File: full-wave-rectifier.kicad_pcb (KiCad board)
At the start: 2 copper layers, 80.6 x 108 mm, 0 parts

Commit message: save changes
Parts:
- added C1: 10uF, Capacitor_THT:CP_Radial_D5.0mm_P2.00mm, B.Cu at (171.4, 137.2)
- added C10: 100nF, Capacitor_SMD:C_1206_3216Metric, F.Cu at (184.2, 68.6)
- added C11: 100nF, Capacitor_SMD:C_1206_3216Metric, F.Cu at (171.4, 101.6)
- added C12: 100nF, Capacitor_SMD:C_1206_3216Metric, F.Cu at (184.2, 101.6)
- added C13: 100nF, Capacitor_SMD:C_1206_3216Metric, F.Cu at (171.4, 127.0)
- added C14: 100nF, Capacitor_SMD:C_1206_3216Metric, F.Cu at (184.2, 127.0)
- added C15: 1uF_Radial_TH, Capacitor_THT:C_Rect_L7.2mm_W4.5mm_P5.00mm_FKS2_FKP2_MKS2_MKP2, F.Cu at (207.4, 77.5)
- added C2: 10uF, Capacitor_THT:CP_Radial_D5.0mm_P2.00mm, B.Cu at (182.2, 137.2)
- added C3: 10uF, Capacitor_THT:CP_Radial_D5.0mm_P2.00mm, F.Cu at (201.3, 68.4)
- added C4: 10uF, Capacitor_THT:CP_Radial_D5.0mm_P2.00mm, F.Cu at (201.3, 75.0)
- added C5: 100nF, Capacitor_SMD:C_1206_3216Metric, F.Cu at (165.1, 142.0)
- added C6: 100nF, Capacitor_SMD:C_1206_3216Metric, F.Cu at (190.5, 142.0)
- added C7: 100nF, Capacitor_THT:C_Disc_D4.3mm_W1.9mm_P5.00mm, F.Cu at (215.9, 76.2)
- added C8: 100nF, Capacitor_THT:C_Disc_D4.3mm_W1.9mm_P5.00mm, F.Cu at (215.9, 79.7)
- added C9: 100nF, Capacitor_SMD:C_1206_3216Metric, F.Cu at (171.4, 68.6)
- added D3: 1N4148, Diode_THT:D_DO-35_SOD27_P7.62mm_Horizontal, F.Cu at (177.8, 24.4)
- added D4: 1N4148, Diode_THT:D_DO-35_SOD27_P7.62mm_Horizontal, F.Cu at (177.8, 27.9)
- added D5: 1N4148, Diode_THT:D_DO-35_SOD27_P7.62mm_Horizontal, F.Cu at (177.8, 31.5)
- added D6: 1N4148, Diode_THT:D_DO-35_SOD27_P7.62mm_Horizontal, F.Cu at (177.8, 35.0)
- added FB1: FerriteBead, Inductor_SMD:L_1206_3216Metric_Pad1.22x1.90mm_HandSolder, F.Cu at (188.8, 146.1)
- added FB2: FerriteBead, Inductor_SMD:L_1206_3216Metric_Pad1.22x1.90mm_HandSolder, F.Cu at (165.1, 150.7)
- added J10: Control Right, Connector_PinSocket_2.54mm:PinSocket_1x08_P2.54mm_Vertical, B.Cu at (139.7, 94.0)
- added J11: Main Right, Connector_PinHeader_2.54mm:PinHeader_1x08_P2.54mm_Vertical, F.Cu at (190.5, 94.0)
- added J12: Power Connector, Connector_IDC:IDC-Header_2x05_P2.54mm_Vertical, B.Cu at (182.9, 147.3)
- added J2: Input Ch1, AudioJacks:Jack_3.5mm_QingPu_WQP-PJ398SM_Vertical, F.Cu at (121.9, 131.9)
- added J3: Input Ch2, AudioJacks:Jack_3.5mm_QingPu_WQP-PJ398SM_Vertical, F.Cu at (132.1, 131.9)
- added J4: Output Ch1, AudioJacks:Jack_3.5mm_QingPu_WQP-PJ398SM_Vertical, F.Cu at (121.9, 147.2)
- added J5: Output Ch2, AudioJacks:Jack_3.5mm_QingPu_WQP-PJ398SM_Vertical, F.Cu at (132.1, 147.2)
- added J6: Ochd input, Connector_PinHeader_2.54mm:PinHeader_1x02_P2.54mm_Vertical, B.Cu at (139.7, 119.4)
- added J8: Control Left, Connector_PinSocket_2.54mm:PinSocket_1x08_P2.54mm_Vertical, B.Cu at (114.3, 94.0)
- added J9: Main Left, Connector_PinHeader_2.54mm:PinHeader_1x08_P2.54mm_Vertical, F.Cu at (165.1, 94.0)
- added POT1: 9mm_NoDet_10k_DShaft, Potentiometer_THT:Potentiometer_Alpha_RD901F-40-00D_Single_Vertical, F.Cu at (124.5, 61.0)
- added POT2: 9mm_NoDet_10k_DShaft, Potentiometer_THT:Potentiometer_Alpha_RD901F-40-00D_Single_Vertical, F.Cu at (124.5, 81.3)
- added POT3: 9mm_NoDet_10k_DShaft, Potentiometer_THT:Potentiometer_Alpha_RD901F-40-00D_Single_Vertical, F.Cu at (124.5, 101.6)
- added POT4: 9mm_NoDet_10k_DShaft, Potentiometer_THT:Potentiometer_Alpha_RD901F-40-00D_Single_Vertical, F.Cu at (124.5, 121.9)
- added Q7: AO3404A, Package_TO_SOT_SMD:SOT-23_Handsoldering, F.Cu at (184.4, 151.4)
- added Q8: AO3407A, Package_TO_SOT_SMD:SOT-23_Handsoldering, F.Cu at (171.2, 151.4)
- added R1: 100k, Resistor_SMD:R_1206_3216Metric, F.Cu at (168.9, 145.9)
- added R10: 100k_TH0.125, Resistor_THT:R_Axial_DIN0207_L6.3mm_D2.5mm_P2.54mm_Vertical, F.Cu at (86.6, 39.9)
- added R11: 100k_TH0.125, Resistor_THT:R_Axial_DIN0207_L6.3mm_D2.5mm_P2.54mm_Vertical, F.Cu at (86.6, 43.9)
- added R12: 100k_TH0.125, Resistor_THT:R_Axial_DIN0207_L6.3mm_D2.5mm_P2.54mm_Vertical, F.Cu at (92.7, 27.7)
- added R13: 100k_TH0.125, Resistor_THT:R_Axial_DIN0207_L6.3mm_D2.5mm_P2.54mm_Vertical, F.Cu at (92.7, 31.8)
- added R14: 100k_TH0.125, Resistor_THT:R_Axial_DIN0207_L6.3mm_D2.5mm_P2.54mm_Vertical, F.Cu at (92.7, 35.8)
- added R15: 100k_TH0.125, Resistor_THT:R_Axial_DIN0207_L6.3mm_D2.5mm_P2.54mm_Vertical, F.Cu at (92.7, 39.9)
- added R16: 100k_TH0.125, Resistor_THT:R_Axial_DIN0207_L6.3mm_D2.5mm_P2.54mm_Vertical, F.Cu at (92.7, 43.9)
- added R17: 100k_TH0.125, Resistor_THT:R_Axial_DIN0207_L6.3mm_D2.5mm_P2.54mm_Vertical, F.Cu at (98.8, 27.7)
- added R18: 100k_TH0.125, Resistor_THT:R_Axial_DIN0207_L6.3mm_D2.5mm_P2.54mm_Vertical, F.Cu at (98.8, 31.8)
- added R19: 100k_TH0.125, Resistor_THT:R_Axial_DIN0207_L6.3mm_D2.5mm_P2.54mm_Vertical, F.Cu at (98.8, 35.8)
- added R2: 100k, Resistor_SMD:R_1206_3216Metric, F.Cu at (190.5, 150.9)
- added R20: 100k_TH0.125, Resistor_THT:R_Axial_DIN0207_L6.3mm_D2.5mm_P2.54mm_Vertical, F.Cu at (98.8, 39.9)
- added R21: 51k_TH0.125, Resistor_THT:R_Axial_DIN0207_L6.3mm_D2.5mm_P5.08mm_Vertical, F.Cu at (160.0, 33.3)
- added R22: 51k_TH0.125, Resistor_THT:R_Axial_DIN0207_L6.3mm_D2.5mm_P5.08mm_Vertical, F.Cu at (160.0, 37.3)
- added R23: 100Ω_TH0.125, Resistor_THT:R_Axial_DIN0207_L6.3mm_D2.5mm_P2.54mm_Vertical, F.Cu at (207.6, 82.5)
- added R3: 100k_TH0.125, Resistor_THT:R_Axial_DIN0207_L6.3mm_D2.5mm_P2.54mm_Vertical, F.Cu at (108.0, 134.6)
- added R4: 100k_TH0.125, Resistor_THT:R_Axial_DIN0207_L6.3mm_D2.5mm_P2.54mm_Vertical, F.Cu at (134.6, 106.7)
- added R5: 1k_TH0.125, Resistor_THT:R_Axial_DIN0207_L6.3mm_D2.5mm_P5.08mm_Vertical, F.Cu at (105.4, 129.5)
- added R6: 1k_TH0.125, Resistor_THT:R_Axial_DIN0207_L6.3mm_D2.5mm_P5.08mm_Vertical, F.Cu at (134.6, 116.6)
- added R7: 1k_TH0.125, Resistor_THT:R_Axial_DIN0207_L6.3mm_D2.5mm_P5.08mm_Vertical, F.Cu at (103.1, 152.4)
- added R8: 1k_TH0.125, Resistor_THT:R_Axial_DIN0207_L6.3mm_D2.5mm_P5.08mm_Vertical, F.Cu at (143.7, 152.4)
- added R9: 100k_TH0.125, Resistor_THT:R_Axial_DIN0207_L6.3mm_D2.5mm_P2.54mm_Vertical, F.Cu at (86.6, 35.8)
- added U1: LM78L05_TO92, Package_TO_SOT_THT:TO-92_Inline_Wide, F.Cu at (219.1, 64.9)
- added U2: TL074, Package_SO:SOIC-14_3.9x8.7mm_P1.27mm, F.Cu at (177.8, 127.0)
- added U3: TL074, Package_SO:SOIC-14_3.9x8.7mm_P1.27mm, F.Cu at (177.8, 101.6)
- added U4: TL074, Package_SO:SOIC-14_3.9x8.7mm_P1.27mm, F.Cu at (177.8, 68.6)
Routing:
- net +12V: track 0.00 -> 100.9 mm
- net -12V: track 0.00 -> 97.9 mm
- net Net-(Q8-D): track 0.00 -> 6.67 mm
- net Net-(Q7-D): track 0.00 -> 6.67 mm
- net Net-(Q7-S): track 0.00 -> 4.99 mm
- net Net-(Q8-S): track 0.00 -> 4.62 mm
- net Net-(Q7-G): track 0.00 -> 4.62 mm
- net Net-(Q8-G): track 0.00 -> 3.52 mm
- added copper zone on B.Cu, net GND
- added copper zone on F.Cu, net GND
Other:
- outline, holes or cut-outs redrawn

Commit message: save changes
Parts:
- moved R7 37.4 mm to (118.1, 118.1), turned to -90 degrees
- moved R8 35.2 mm to (135.9, 118.1), turned to -90 degrees
- moved R3 31.2 mm to (121.9, 106.7)
- moved R5 19.8 mm to (118.1, 114.3), turned to 90 degrees
- moved R6 2.64 mm to (135.9, 114.3)
- moved R4 2.54 mm to (132.1, 106.7)
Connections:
- POT1 pad 1: /T_Output_1 -> Net-(POT1A-Left)
- POT2 pad 1: /T_Offset_1 -> Net-(POT2A-Left)
- POT3 pad 1: /T_Output_2 -> Net-(POT3A-Left)
- POT4 pad 1: /T_Offset_2 -> Net-(POT4A-Left)
- R13 pad 1: INPUT_CH1 -> Net-(U3D--)
- R14 pad 2: INPUT_CH1 -> Net-(U3D--)
- R16 pad 1: INPUT_CH2 -> Net-(U3B--)
- R17 pad 2: INPUT_CH2 -> Net-(U3B--)
- R19 pad 2: /B_Output_1 -> Net-(POT1A-Left)
- R20 pad 2: /B_Output_2 -> Net-(POT3A-Left)
- R5 pad 2: Net-(U3D-+) -> INPUT_CH1
- R6 pad 2: Net-(U3B-+) -> INPUT_CH2
- R7 pad 1: Net-(U3A--) -> OUTPUT_CH1
- R8 pad 1: Net-(U3C--) -> OUTPUT_CH2
- U2 pad 1: /B_Offset_1 -> Net-(POT2A-Left)
- U2 pad 2: /B_Offset_1 -> Net-(POT2A-Left)
- U2 pad 6: /B_Offset_2 -> Net-(POT4A-Left)
- U2 pad 7: /B_Offset_2 -> Net-(POT4A-Left)
- U3 pad 1: Net-(U3A--) -> OUTPUT_CH1
- U3 pad 12: Net-(U3D-+) -> INPUT_CH1
- U3 pad 13: INPUT_CH1 -> Net-(U3D--)
- U3 pad 14: INPUT_CH1 -> Net-(U3D--)
- U3 pad 2: Net-(U3A--) -> OUTPUT_CH1
- U3 pad 5: Net-(U3B-+) -> INPUT_CH2
- U3 pad 6: INPUT_CH2 -> Net-(U3B--)
- U3 pad 7: INPUT_CH2 -> Net-(U3B--)
- U3 pad 8: Net-(U3C--) -> OUTPUT_CH2
- U3 pad 9: Net-(U3C--) -> OUTPUT_CH2
- U4 pad 1: /B_Output_1 -> Net-(POT1A-Left)
- U4 pad 14: /B_Output_2 -> Net-(POT3A-Left)
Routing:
- net OCHD_CH1: track 0.00 -> 26.7 mm
- net Net-(J2-PadT): track 0.00 -> 23.5 mm
- net Net-(J3-PadT): track 0.00 -> 23.5 mm
- net Net-(J4-PadT): track 0.00 -> 20.6 mm
- net Net-(J5-PadT): track 0.00 -> 20.6 mm
- net OCHD_CH2: track 0.00 -> 16.5 mm
- net OUTPUT_CH2: track 0.00 -> 7.93 mm
- net OUTPUT_CH1: track 0.00 -> 7.93 mm
- net INPUT_CH2: track 0.00 -> 3.81 mm
- net INPUT_CH1: track 0.00 -> 3.81 mm

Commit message: power
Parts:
- C15, C3, C4: moved to B.Cu
- C7, C8: footprint Capacitor_THT:C_Disc_D4.3mm_W1.9mm_P5.00mm -> Capacitor_SMD:C_1206_3216Metric_Pad1.33x1.80mm_HandSolder
- R23: footprint Resistor_THT:R_Axial_DIN0207_L6.3mm_D2.5mm_P2.54mm_Vertical -> Resistor_SMD:R_1206_3216Metric_Pad1.30x1.75mm_HandSolder
- moved U1 78.7 mm to (180.3, 133.3), turned to 180 degrees
- moved C3 72.8 mm to (168.4, 133.3), turned to 180 degrees
- moved C7 70.4 mm to (172.7, 131.8), turned to 90 degrees
- moved C8 61.7 mm to (182.9, 131.8), turned to 90 degrees
- moved C4 60.2 mm to (186.7, 133.3)
- moved C15 55.5 mm to (177.8, 124.5), turned to -90 degrees
- moved R23 48.2 mm to (186.7, 126.0), turned to 90 degrees
- moved C13 10.2 mm to (171.4, 116.8)
- moved C14 10.2 mm to (184.2, 116.8)
- moved U2 10.2 mm to (177.8, 116.8)
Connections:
- U2 pad 12: GND -> +5V
- U2 pad 13: Net-(U2D--) -> Net-(POT4A-Left)
- U2 pad 14: Net-(U2D--) -> Net-(POT4A-Left)
- U2 pad 5: +5V -> GND
- U2 pad 6: Net-(POT4A-Left) -> Net-(U2B--)
- U2 pad 7: Net-(POT4A-Left) -> Net-(U2B--)
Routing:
- net +5V: track 0.00 -> 22.5 mm
- net +12V: track 100.9 -> 119.3 mm, vias 0 -> 2
- net Net-(U1-VO): track 0.00 -> 12.1 mm
- net -12V: track 97.9 -> 101.8 mm, vias 0 -> 1
- net Net-(U2C--): track 0.00 -> 1.27 mm
- net Net-(U2B--): track 0.00 -> 1.27 mm
- net Net-(POT4A-Left): track 0.00 -> 1.27 mm
- net Net-(POT2A-Left): track 0.00 -> 1.27 mm

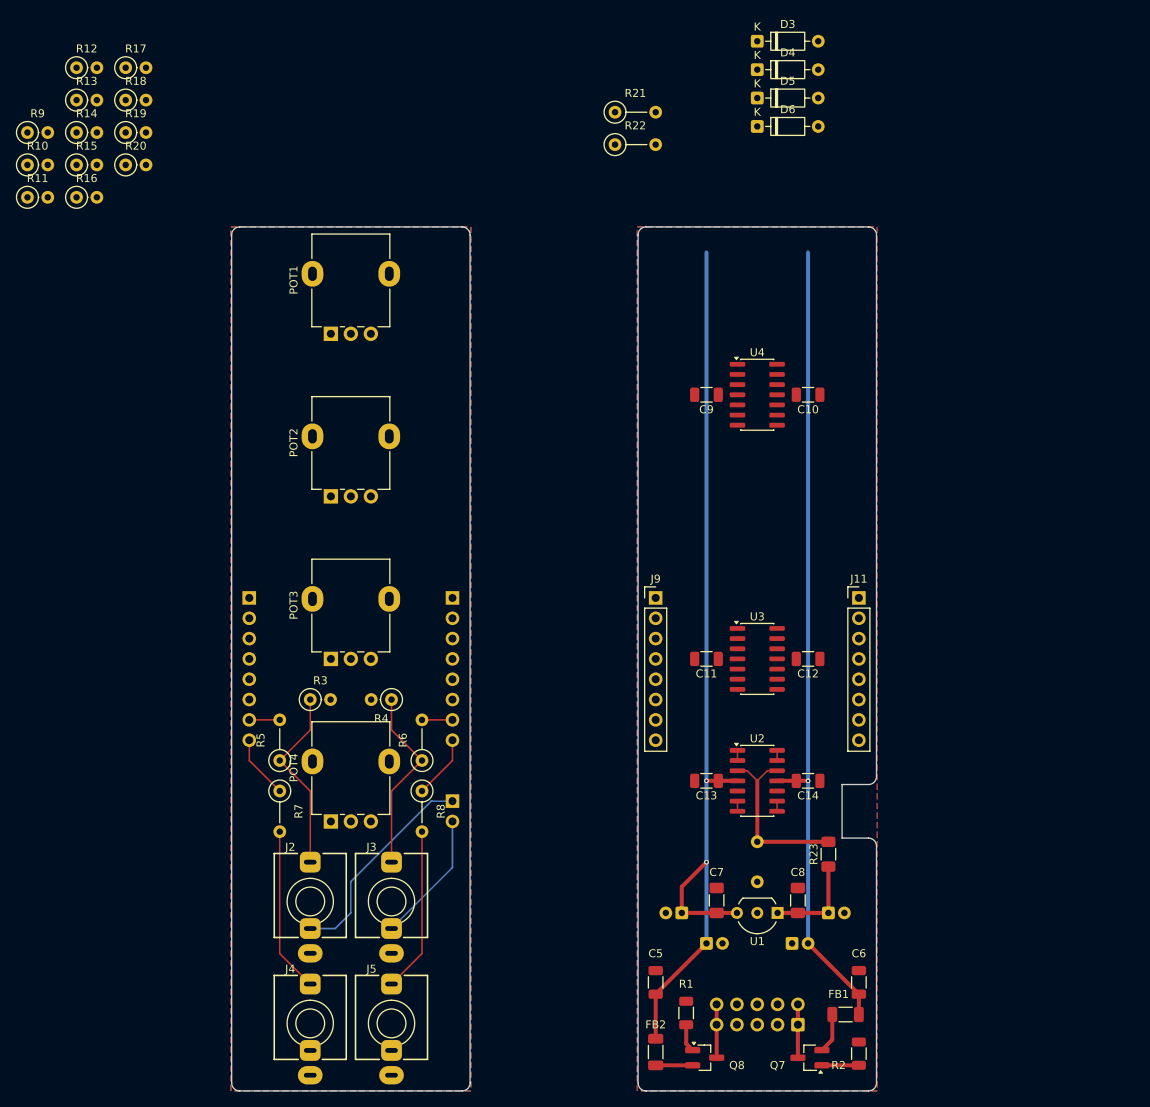
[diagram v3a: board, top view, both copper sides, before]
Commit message: added rectifiers
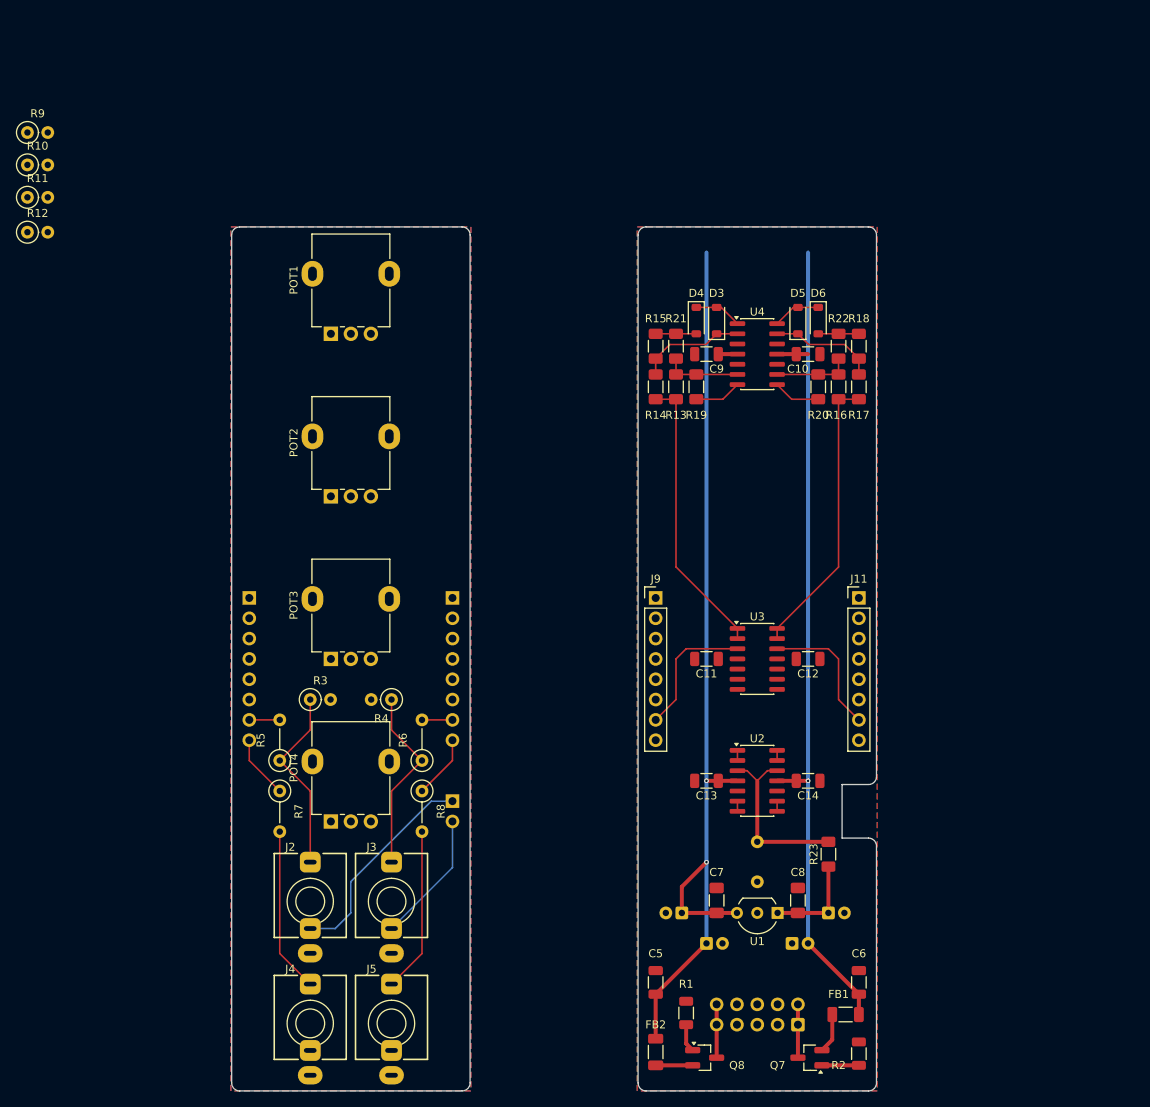
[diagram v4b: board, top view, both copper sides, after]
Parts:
- D3, D4, D5, D6: footprint Diode_THT:D_DO-35_SOD27_P7.62mm_Horizontal -> Diode_SMD:D_SOD-123
- R13, R14, R15, R16, R17, R18, R19, R20: footprint Resistor_THT:R_Axial_DIN0207_L6.3mm_D2.5mm_P2.54mm_Vertical -> Resistor_SMD:R_1206_3216Metric_Pad1.30x1.75mm_HandSolder
- R21, R22: footprint Resistor_THT:R_Axial_DIN0207_L6.3mm_D2.5mm_P5.08mm_Vertical -> Resistor_SMD:R_1206_3216Metric_Pad1.30x1.75mm_HandSolder
- moved R17 100.0 mm to (190.5, 67.6), turned to -90 degrees
- moved R16 98.2 mm to (188.0, 67.6), turned to 90 degrees
- moved R18 96.7 mm to (190.5, 62.5), turned to 90 degrees
- moved R20 90.9 mm to (185.4, 67.6), turned to -90 degrees
- moved R13 83.1 mm to (167.6, 67.6), turned to 90 degrees
- moved R14 79.1 mm to (165.1, 67.6), turned to -90 degrees
- moved R19 78.1 mm to (170.2, 67.6), turned to -90 degrees
- moved R15 75.9 mm to (165.1, 62.5), turned to 90 degrees
- moved R22 37.6 mm to (188.0, 62.5), turned to 90 degrees
- moved D3 35.3 mm to (172.7, 59.3), turned to 90 degrees
- moved D4 32.3 mm to (170.2, 59.3), turned to -90 degrees
- moved R21 30.2 mm to (167.6, 62.5), turned to 90 degrees
- moved D5 28.3 mm to (182.9, 59.3), turned to 90 degrees
- moved D6 25.4 mm to (185.4, 59.3), turned to -90 degrees
- moved R12 21.5 mm to (86.6, 48.3)
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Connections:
- R10 pad 1: Net-(U3A-+) -> Net-(U3B-+)
- R13 pad 1: Net-(U3D--) -> Net-(U3A--)
- R13 pad 2: Net-(U4A--) -> Net-(U4B--)
- R14 pad 2: Net-(U3D--) -> Net-(U3A--)
- R16 pad 1: Net-(U3B--) -> Net-(U3D--)
- R16 pad 2: Net-(U4D--) -> Net-(U4C--)
- R17 pad 2: Net-(U3B--) -> Net-(U3D--)
- R19 pad 1: Net-(U4A--) -> Net-(U4B--)
- R20 pad 1: Net-(U4D--) -> Net-(U4C--)
- R21 pad 1: Net-(U4A--) -> Net-(U4B--)
- R22 pad 1: Net-(U4D--) -> Net-(U4C--)
- R9 pad 2: Net-(U3A-+) -> Net-(U3B-+)
- U3 pad 1: OUTPUT_CH1 -> Net-(U3A--)
- U3 pad 12: INPUT_CH1 -> INPUT_CH2
- U3 pad 2: OUTPUT_CH1 -> Net-(U3A--)
- U3 pad 3: Net-(U3A-+) -> INPUT_CH1
- U3 pad 5: INPUT_CH2 -> Net-(U3B-+)
- U3 pad 6: Net-(U3B--) -> OUTPUT_CH1
- U3 pad 7: Net-(U3B--) -> OUTPUT_CH1
- U4 pad 1: Net-(POT1A-Left) -> Net-(D3-A)
- U4 pad 13: Net-(U4D--) -> Net-(D5-K)
- U4 pad 14: Net-(POT3A-Left) -> Net-(D5-A)
- U4 pad 2: Net-(U4A--) -> Net-(D3-K)
- U4 pad 6: Net-(D3-K) -> Net-(U4B--)
- U4 pad 7: Net-(D3-A) -> Net-(POT1A-Left)
- U4 pad 8: Net-(D5-A) -> Net-(POT3A-Left)
- U4 pad 9: Net-(D5-K) -> Net-(U4C--)
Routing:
- net Net-(U3D--): track 0.00 -> 35.6 mm
- net Net-(U3A--): track 0.00 -> 35.6 mm
- net INPUT_CH2: track 3.81 -> 20.7 mm
- net INPUT_CH1: track 3.81 -> 20.7 mm
- net Net-(D5-K): track 0.00 -> 13.5 mm
- net Net-(D3-K): track 0.00 -> 13.5 mm
- net Net-(U4C--): track 0.00 -> 9.67 mm
- net Net-(U4B--): track 0.00 -> 9.67 mm
- net Net-(D5-A): track 0.00 -> 5.99 mm
- net Net-(D3-A): track 0.00 -> 5.99 mm
- net Net-(POT3A-Left): track 0.00 -> 5.90 mm
- net Net-(POT1A-Left): track 0.00 -> 5.90 mm
- net Net-(D6-A): track 0.00 -> 5.08 mm
- net Net-(D4-A): track 0.00 -> 5.08 mm
- net -12V: track 101.8 -> 105.6 mm
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
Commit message: save changes
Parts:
- R10, R11, R12, R3, R4, R9: footprint Resistor_THT:R_Axial_DIN0207_L6.3mm_D2.5mm_P2.54mm_Vertical -> Resistor_SMD:R_1206_3216Metric_Pad1.30x1.75mm_HandSolder
- R5, R6, R7, R8: footprint Resistor_THT:R_Axial_DIN0207_L6.3mm_D2.5mm_P5.08mm_Vertical -> Resistor_SMD:R_1206_3216Metric_Pad1.30x1.75mm_HandSolder
- moved R10 62.4 mm to (129.5, 85.1)
- moved R9 60.7 mm to (121.9, 85.1)
- moved R12 56.6 mm to (101.6, 102.9), turned to 180 degrees
- moved R11 54.8 mm to (96.5, 97.8), turned to 180 degrees
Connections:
- J10 pad 1: OFFSET_CH2 -> AMP_CH2
- J10 pad 2: GND -> OFFSET_CH2
- J10 pad 3: GND -> SUM_CH2
- J11 pad 1: OFFSET_CH2 -> AMP_CH2
- J11 pad 2: GND -> OFFSET_CH2
- J11 pad 3: GND -> SUM_CH2
- J8 pad 1: OFFSET_CH1 -> AMP_CH1
- J8 pad 2: GND -> OFFSET_CH1
- J8 pad 3: GND -> SUM_CH1
- J9 pad 1: OFFSET_CH1 -> AMP_CH1
- J9 pad 2: GND -> OFFSET_CH1
- J9 pad 3: GND -> SUM_CH1
- POT1 pad 1: Net-(POT1A-Left) -> AMP_CH1
- POT2 pad 1: Net-(POT2A-Left) -> OFFSET_CH1
- POT3 pad 1: Net-(POT3A-Left) -> AMP_CH2
- POT4 pad 1: Net-(POT4A-Left) -> OFFSET_CH2
- R10 pad 1: Net-(U3B-+) -> SUM_CH1
- R11 pad 2: Net-(U3C-+) -> SUM_CH2
- R12 pad 1: Net-(U3C-+) -> SUM_CH2
- R19 pad 2: Net-(POT1A-Left) -> AMP_CH1
- R20 pad 2: Net-(POT3A-Left) -> AMP_CH2
- R9 pad 2: Net-(U3B-+) -> SUM_CH1
- U2 pad 1: Net-(POT2A-Left) -> OFFSET_CH1
- U2 pad 13: Net-(POT4A-Left) -> OFFSET_CH2
- U2 pad 14: Net-(POT4A-Left) -> OFFSET_CH2
- U2 pad 2: Net-(POT2A-Left) -> OFFSET_CH1
- U3 pad 10: Net-(U3C-+) -> SUM_CH2
- U3 pad 5: Net-(U3B-+) -> SUM_CH1
- U4 pad 7: Net-(POT1A-Left) -> AMP_CH1
- U4 pad 8: Net-(POT3A-Left) -> AMP_CH2
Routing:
- net AMP_CH1: track 0.00 -> 72.3 mm, vias 0 -> 1
- net OFFSET_CH2: track 0.00 -> 59.6 mm, vias 0 -> 1
- net OFFSET_CH1: track 0.00 -> 45.3 mm, vias 0 -> 1
- net SUM_CH1: track 0.00 -> 35.1 mm, vias 0 -> 1
- net Net-(POT1A-Center): track 0.00 -> 26.9 mm
- net OUTPUT_CH1: track 7.93 -> 22.1 mm
- net Net-(POT2A-Center): track 0.00 -> 6.66 mm
- net Net-(POT3A-Left): track 5.90 -> 0.00 mm
- net Net-(POT1A-Left): track 5.90 -> 0.00 mm
- net AMP_CH2: track 0.00 -> 5.90 mm
- net Net-(POT4A-Left): track 1.27 -> 0.00 mm
- net Net-(POT2A-Left): track 1.27 -> 0.00 mm

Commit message: save changes
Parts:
- moved R11 32.7 mm to (128.6, 104.1), turned to 0 degrees
- moved R12 27.2 mm to (128.6, 106.7)
- moved J6 25.9 mm to (114.3, 124.5), turned to 0 degrees
- moved R9 21.9 mm to (125.5, 63.5), turned to 180 degrees
- moved R10 19.5 mm to (125.5, 66.0)
- moved R5 7.95 mm to (120.4, 106.7), turned to 180 degrees
- moved R6 7.78 mm to (134.3, 106.7), turned to 0 degrees
- moved C11 7.62 mm to (171.4, 94.0)
- moved C12 7.62 mm to (184.2, 94.0)
- moved U3 7.62 mm to (177.8, 94.0)
- moved R7 5.19 mm to (114.3, 114.6)
- moved R8 5.19 mm to (139.7, 114.6)
- moved R4 3.40 mm to (134.3, 104.1), turned to 0 degrees
- moved R3 2.98 mm to (120.4, 104.1), turned to 180 degrees
- moved J10 2.54 mm to (139.7, 91.4)
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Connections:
- J10 pad 1: AMP_CH2 -> OFFSET_CH2
- J10 pad 2: OFFSET_CH2 -> AMP_CH2
- J11 pad 1: AMP_CH2 -> OFFSET_CH2
- J11 pad 2: OFFSET_CH2 -> AMP_CH2
- J8 pad 2: OFFSET_CH1 -> SUM_CH1
- J8 pad 3: SUM_CH1 -> OFFSET_CH1
- J9 pad 2: OFFSET_CH1 -> SUM_CH1
- J9 pad 3: SUM_CH1 -> OFFSET_CH1
- POT1 pad : (no net) -> GND
- POT2 pad : (no net) -> GND
- POT3 pad : (no net) -> GND
- POT4 pad : (no net) -> GND
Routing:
- net AMP_CH2: track 5.90 -> 51.4 mm, vias 0 -> 2
- net SUM_CH2: track 0.00 -> 26.0 mm
- net Net-(POT1A-Center): track 26.9 -> 2.54 mm
- net Net-(POT4A-Center): track 0.00 -> 15.2 mm
- net SUM_CH1: track 35.1 -> 48.1 mm, vias 1 -> 0
- net OUTPUT_CH2: track 7.93 -> 20.7 mm
- net OFFSET_CH2: track 59.6 -> 72.2 mm
- net GND: track 0.00 -> 11.8 mm, vias 0 -> 25
- net OCHD_CH2: track 16.5 -> 27.2 mm
- net -12V: track 105.6 -> 96.8 mm, vias 1 -> 3
- net Net-(J4-PadT): track 20.6 -> 29.3 mm
- net Net-(J5-PadT): track 20.6 -> 29.3 mm
- net Net-(POT2A-Center): track 6.66 -> 15.2 mm
- net Net-(U3D--): track 35.6 -> 28.0 mm
- net Net-(U3A--): track 35.6 -> 28.0 mm
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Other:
- outline, holes or cut-outs redrawn

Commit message: Save changes
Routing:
- net GND: vias 25 -> 29
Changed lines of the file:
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@@
+	)
+	(via
+		(at 132.08 100.33)
+		(size 0.6)
+		(drill 0.3)
+		(layers "F.Cu" "B.Cu")
+		(free yes)
+		(net 1)
 	)
 	(via
@@
 	)
 	(via
+		(at 121.92 109.22)
+		(size 0.6)
+		(drill 0.3)
+		(layers "F.Cu" "B.Cu")
+		(free yes)
+		(net 1)
+	)
+	(via
 		(at 177.8 101.6)
 		(size 0.6)
@@
 	)
 	(via
+		(at 121.92 100.33)
+		(size 0.6)
+		(drill 0.3)
+		(layers "F.Cu" "B.Cu")
+		(free yes)
+		(net 1)
+	)
+	(via
 		(at 167.64 53.975)
 		(size 0.6)
@@
 	(via
 		(at 132.08 64.77)
+		(size 0.6)
+		(drill 0.3)
+		(layers "F.Cu" "B.Cu")
+		(free yes)
+		(net 1)
+	)
+	(via
+		(at 132.08 109.22)
 		(size 0.6)
 		(drill 0.3)
@@
 		(polygon
 			(pts
-				(xy 162.941 47.625) (xy 192.659 47.625) (xy 192.659 155.575) (xy 192.659 155.575) (xy 162.941 155.575)
-				(xy 162.941 126.365) (xy 167.005 126.365) (xy 167.005 120.015) (xy 162.941 120.015)
+				(xy 162.941 47.625) (xy 192.659 47.625) (xy 192.659 155.575) (xy 162.941 155.575) (xy 162.941 126.365)
+				(xy 167.005 126.365) (xy 167.005 120.015) (xy 162.941 120.015)
 			)
 		)
